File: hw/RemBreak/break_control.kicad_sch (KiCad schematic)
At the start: 13 parts, among them J1 Conn_01x03, J8 Conn_01x07, J9 Conn_01x07, Q1 BC337, Q2 BC847

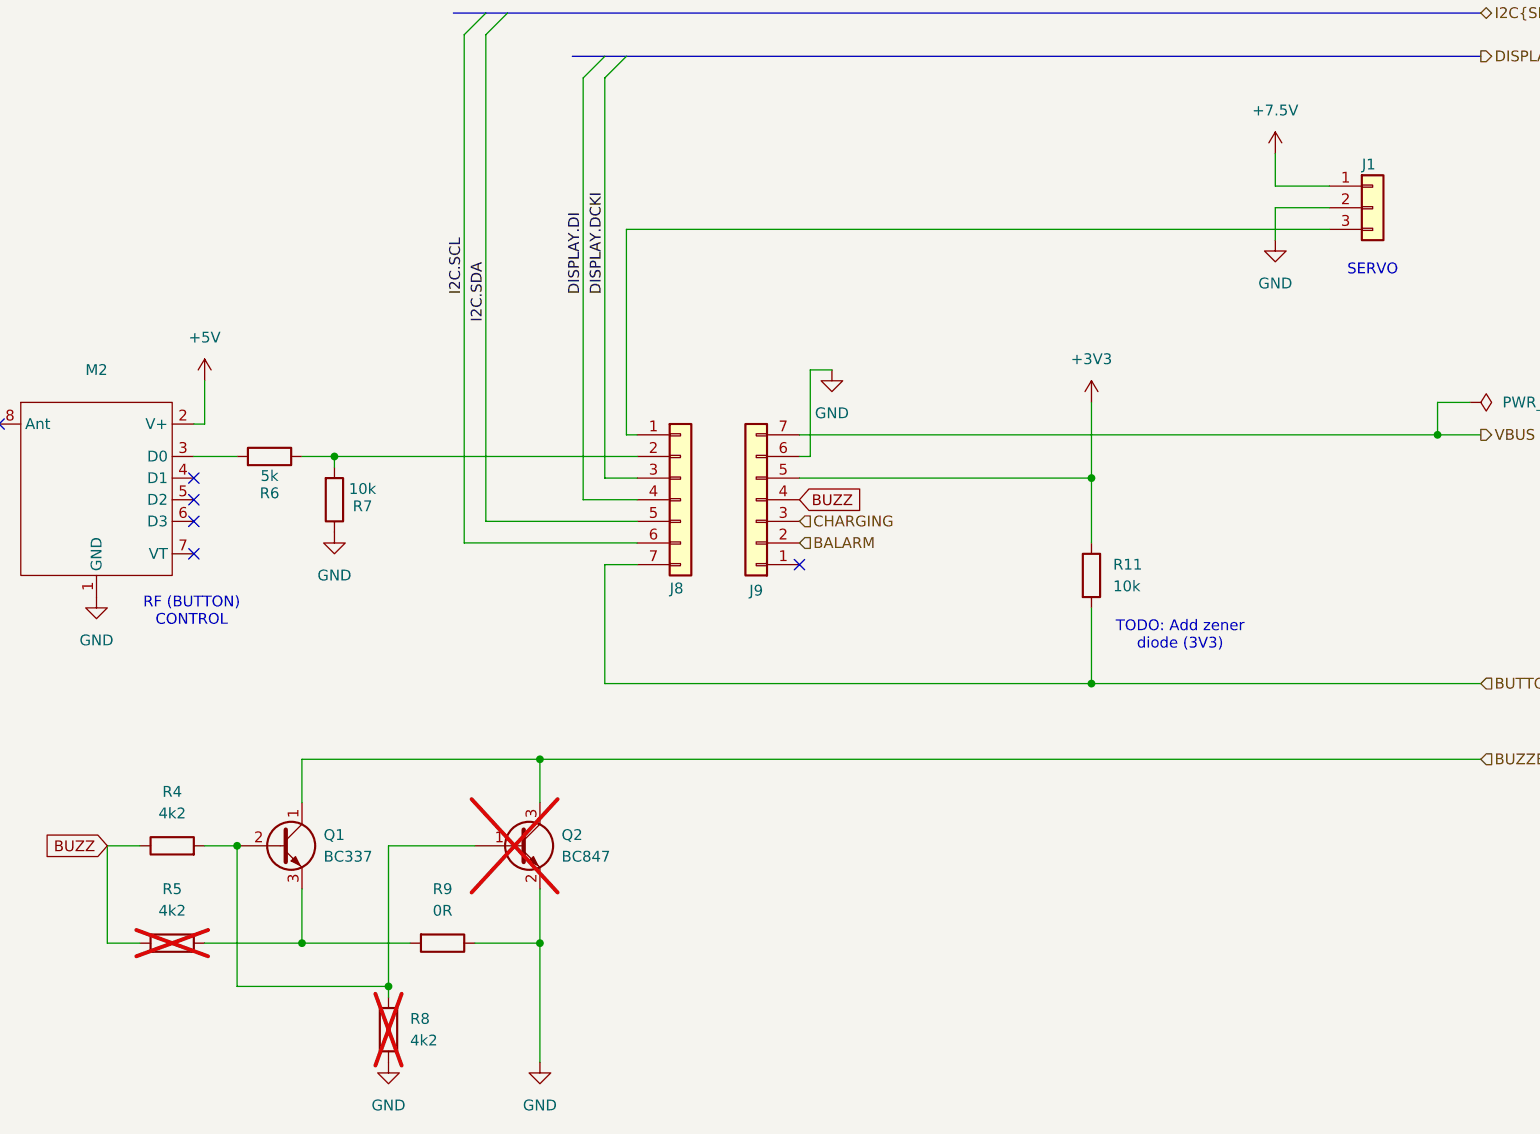
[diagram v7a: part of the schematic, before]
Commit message: regenerated anotations and used battery connector with grounding
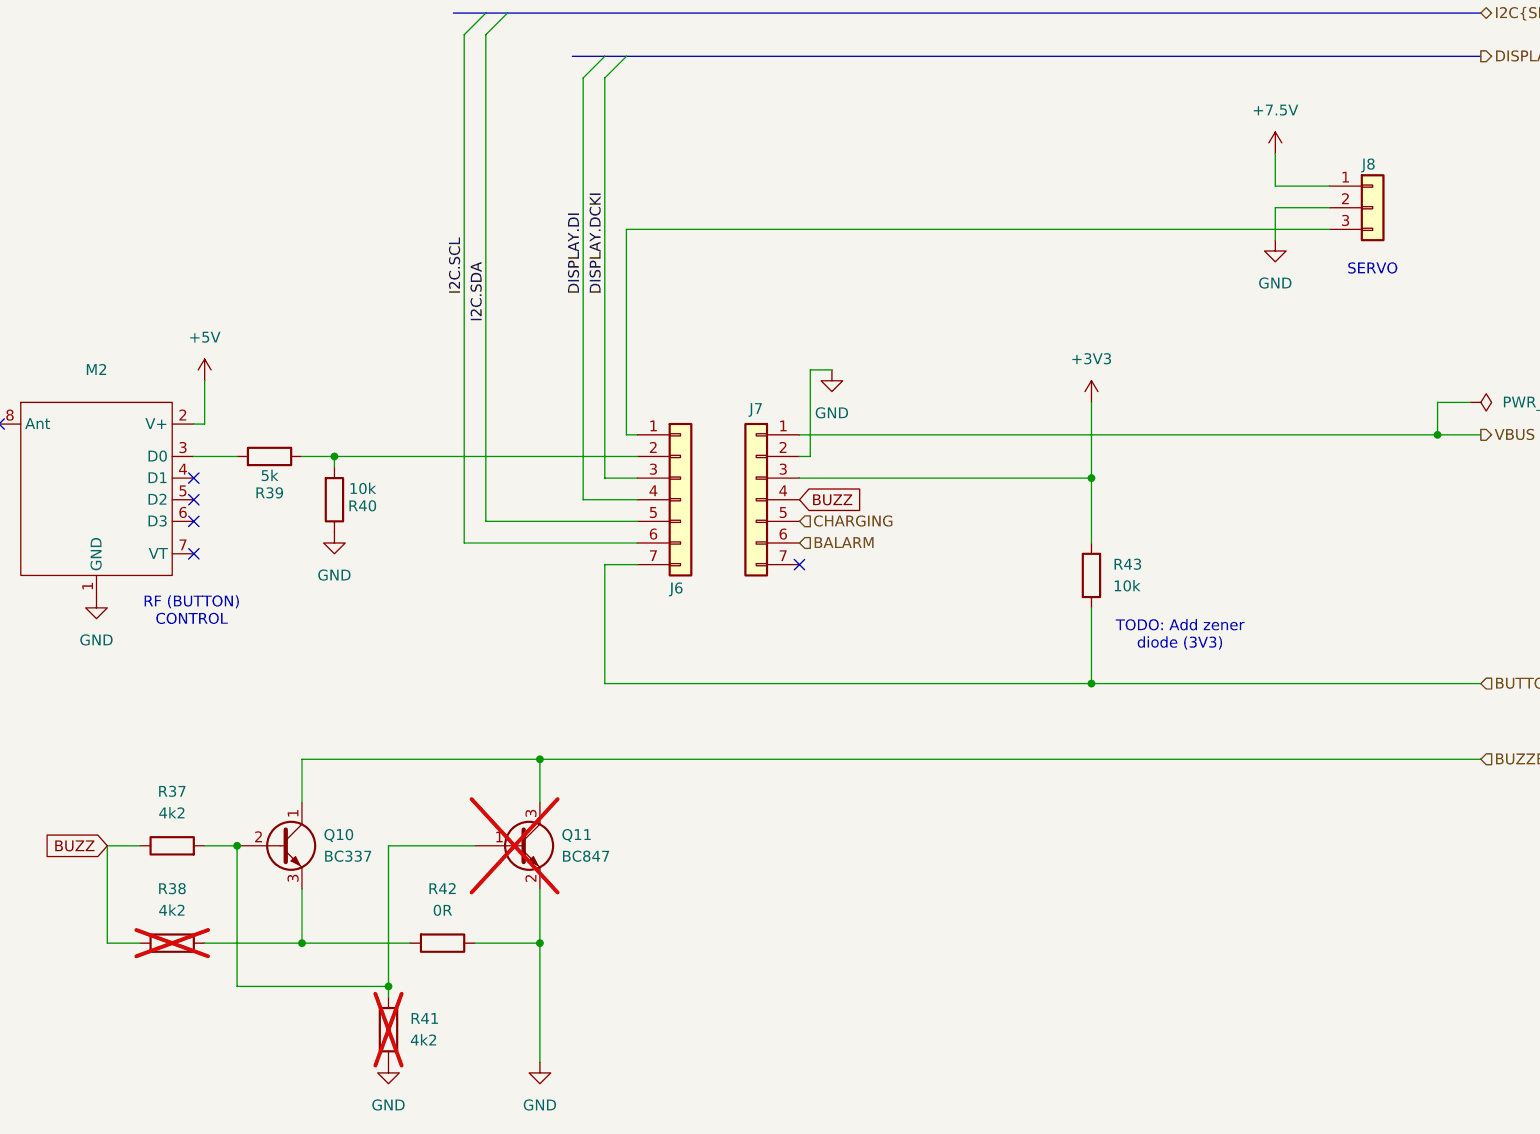
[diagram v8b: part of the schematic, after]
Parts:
- renumbered J8 to J6, J9 to J7, J1 to J8, Q1 to Q10, Q2 to Q11, R4 to R37, R5 to R38, R6 to R39, R7 to R40, R8 to R41, R9 to R42, R11 to R43
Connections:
- net +3V3: now also J7.3 (Pin_3); no longer J7.5 (Pin_5)
- net BALARM: now also J7.6 (Pin_6); no longer J7.2 (Pin_2)
- net CHARGING: now also J7.5 (Pin_5); no longer J7.3 (Pin_3)
- net GND: now also J7.2 (Pin_2); no longer J7.6 (Pin_6)
- net VBUS: now also J7.1 (Pin_1); no longer J7.7 (Pin_7)
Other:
- moved on the sheet: J7
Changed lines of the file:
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@@
 		(on_board yes)
 		(dnp no)
-		(property "Reference" "J1"
+		(property "Reference" "J8"
 			(at 214.63 54.61 0)
 			(effects
@@
 			(project "RemBreak"
 				(path "/e6d4ae5b-c9d7-4cbe-b288-c929fdf55a75/4813b76c-f465-42f9-8515-5ce5d55b4403"
-					(reference "J1")
+					(reference "J8")
 					(unit 1)
 				)
@@
 		(dnp no)
 		(fields_autoplaced yes)
-		(property "Reference" "Q1"
+		(property "Reference" "Q10"
 			(at 92.71 133.3499 0)
 			(effects
@@
 			(project "RemBreak"
 				(path "/e6d4ae5b-c9d7-4cbe-b288-c929fdf55a75/4813b76c-f465-42f9-8515-5ce5d55b4403"
-					(reference "Q1")
+					(reference "Q10")
 					(unit 1)
 				)
@@
 		(dnp no)
 		(fields_autoplaced yes)
-		(property "Reference" "#PWR06"
+		(property "Reference" "#PWR040"
 			(at 118.11 166.37 0)
 			(effects
@@
 			(project "RemBreak"
 				(path "/e6d4ae5b-c9d7-4cbe-b288-c929fdf55a75/4813b76c-f465-42f9-8515-5ce5d55b4403"
-					(reference "#PWR06")
+					(reference "#PWR040")
 					(unit 1)
 				)
@@
 		(dnp no)
 		(fields_autoplaced yes)
-		(property "Reference" "R4"
+		(property "Reference" "R37"
 			(at 74.93 128.27 90)
 			(effects
@@
 			(project "RemBreak"
 				(path "/e6d4ae5b-c9d7-4cbe-b288-c929fdf55a75/4813b76c-f465-42f9-8515-5ce5d55b4403"
-					(reference "R4")
+					(reference "R37")
 					(unit 1)
 				)
@@
 		(dnp no)
 		(fields_autoplaced yes)
-		(property "Reference" "R11"
+		(property "Reference" "R43"
 			(at 185.42 101.5999 0)
 			(effects
@@
 			(project "RemBreak"
 				(path "/e6d4ae5b-c9d7-4cbe-b288-c929fdf55a75/4813b76c-f465-42f9-8515-5ce5d55b4403"
-					(reference "R11")
+					(reference "R43")
 					(unit 1)
 				)
@@
 		(dnp no)
 		(fields_autoplaced yes)
-		(property "Reference" "#PWR017"
+		(property "Reference" "#PWR042"
 			(at 182.88 86.36 0)
 			(effects
@@
 			(project ""
 				(path "/e6d4ae5b-c9d7-4cbe-b288-c929fdf55a75/4813b76c-f465-42f9-8515-5ce5d55b4403"
-					(reference "#PWR017")
+					(reference "#PWR042")
 					(unit 1)
 				)
@@
 		(dnp yes)
 		(fields_autoplaced yes)
-		(property "Reference" "Q2"
+		(property "Reference" "Q11"
 			(at 120.65 133.3499 0)
 			(effects
@@
 			(project "RemBreak"
 				(path "/e6d4ae5b-c9d7-4cbe-b288-c929fdf55a75/4813b76c-f465-42f9-8515-5ce5d55b4403"
-					(reference "Q2")
+					(reference "Q11")
 					(unit 1)
 				)
@@
 		(dnp no)
 		(fields_autoplaced yes)
-		(property "Reference" "#PWR022"
+		(property "Reference" "#PWR036"
 			(at 66.04 111.76 0)
 			(effects
@@
 			(project ""
 				(path "/e6d4ae5b-c9d7-4cbe-b288-c929fdf55a75/4813b76c-f465-42f9-8515-5ce5d55b4403"
-					(reference "#PWR022")
+					(reference "#PWR036")
 					(unit 1)
 				)
@@
 	(symbol
 		(lib_id "Connector_Generic:Conn_01x07")
-		(at 143.51 93.98 180)
-		(unit 1)
-		(exclude_from_sim no)
-		(in_bom yes)
-		(on_board yes)
-		(dnp no)
-		(property "Reference" "J9"
-			(at 143.51 104.648 0)
+		(at 143.51 93.98 0)
+		(mirror y)
+		(unit 1)
+		(exclude_from_sim no)
+		(in_bom yes)
+		(on_board yes)
+		(dnp no)
+		(property "Reference" "J7"
+			(at 143.51 83.312 0)
 			(effects
 				(font
@@
 		)
 		(property "Value" "Conn_01x07"
-			(at 143.51 82.55 0)
+			(at 143.51 105.41 0)
 			(effects
 				(font
@@
 			(project "RemBreak"
 				(path "/e6d4ae5b-c9d7-4cbe-b288-c929fdf55a75/4813b76c-f465-42f9-8515-5ce5d55b4403"
-					(reference "J9")
+					(reference "J7")
 					(unit 1)
 				)
@@
 		(dnp no)
 		(fields_autoplaced yes)
-		(property "Reference" "R9"
+		(property "Reference" "R42"
 			(at 106.68 139.7 90)
 			(effects
@@
 			(project "RemBreak"
 				(path "/e6d4ae5b-c9d7-4cbe-b288-c929fdf55a75/4813b76c-f465-42f9-8515-5ce5d55b4403"
-					(reference "R9")
+					(reference "R42")
 					(unit 1)
 				)
@@
 		(dnp no)
 		(fields_autoplaced yes)
-		(property "Reference" "#PWR07"
+		(property "Reference" "#PWR044"
 			(at 204.47 69.85 0)
 			(effects
@@
 			(project "RemBreak"
 				(path "/e6d4ae5b-c9d7-4cbe-b288-c929fdf55a75/4813b76c-f465-42f9-8515-5ce5d55b4403"
-					(reference "#PWR07")
+					(reference "#PWR044")
 					(unit 1)
 				)
@@
 		(dnp no)
 		(fields_autoplaced yes)
-		(property "Reference" "#PWR02"
+		(property "Reference" "#PWR038"
 			(at 93.98 104.14 0)
 			(effects
@@
 			(project "RemBreak"
 				(path "/e6d4ae5b-c9d7-4cbe-b288-c929fdf55a75/4813b76c-f465-42f9-8515-5ce5d55b4403"
-					(reference "#PWR02")
+					(reference "#PWR038")
 					(unit 1)
 				)
@@
 		(dnp yes)
 		(fields_autoplaced yes)
-		(property "Reference" "R5"
+		(property "Reference" "R38"
 			(at 74.93 139.7 90)
 			(effects
@@
 			(project "RemBreak"
 				(path "/e6d4ae5b-c9d7-4cbe-b288-c929fdf55a75/4813b76c-f465-42f9-8515-5ce5d55b4403"
-					(reference "R5")
+					(reference "R38")
 					(unit 1)
 				)
@@
 		(on_board yes)
 		(dnp no)
-		(property "Reference" "J8"
+		(property "Reference" "J6"
 			(at 133.35 104.394 0)
 			(effects
@@
 			(project "RemBreak"
 				(path "/e6d4ae5b-c9d7-4cbe-b288-c929fdf55a75/4813b76c-f465-42f9-8515-5ce5d55b4403"
-					(reference "J8")
+					(reference "J6")
 					(unit 1)
 				)
@@
 		(dnp no)
 		(fields_autoplaced yes)
-		(property "Reference" "#PWR035"
+		(property "Reference" "#PWR037"
 			(at 78.74 83.82 0)
 			(effects
@@
 			(project ""
 				(path "/e6d4ae5b-c9d7-4cbe-b288-c929fdf55a75/4813b76c-f465-42f9-8515-5ce5d55b4403"
-					(reference "#PWR035")
+					(reference "#PWR037")
 					(unit 1)
 				)
@@
 		(dnp no)
 		(fields_autoplaced yes)
-		(property "Reference" "#PWR09"
+		(property "Reference" "#PWR041"
 			(at 152.4 85.09 0)
 			(effects
@@
 			(project "RemBreak"
 				(path "/e6d4ae5b-c9d7-4cbe-b288-c929fdf55a75/4813b76c-f465-42f9-8515-5ce5d55b4403"
-					(reference "#PWR09")
+					(reference "#PWR041")
 					(unit 1)
 				)
@@
 		(dnp no)
 		(fields_autoplaced yes)
-		(property "Reference" "#FLG08"
+		(property "Reference" "#FLG07"
 			(at 229.235 82.55 0)
 			(effects
@@
 			(project "RemBreak"
 				(path "/e6d4ae5b-c9d7-4cbe-b288-c929fdf55a75/4813b76c-f465-42f9-8515-5ce5d55b4403"
-					(reference "#FLG08")
+					(reference "#FLG07")
 					(unit 1)
 				)
@@
 		(dnp no)
 		(fields_autoplaced yes)
-		(property "Reference" "#PWR03"
+		(property "Reference" "#PWR039"
 			(at 100.33 166.37 0)
 			(effects
@@
 			(project "RemBreak"
 				(path "/e6d4ae5b-c9d7-4cbe-b288-c929fdf55a75/4813b76c-f465-42f9-8515-5ce5d55b4403"
-					(reference "#PWR03")
+					(reference "#PWR039")
 					(unit 1)
 				)
@@
 		(dnp yes)
 		(fields_autoplaced yes)
-		(property "Reference" "R8"
+		(property "Reference" "R41"
 			(at 102.87 154.9399 0)
 			(effects
@@
 			(project "RemBreak"
 				(path "/e6d4ae5b-c9d7-4cbe-b288-c929fdf55a75/4813b76c-f465-42f9-8515-5ce5d55b4403"
-					(reference "R8")
+					(reference "R41")
 					(unit 1)
 				)
@@
 		(on_board yes)
 		(dnp no)
-		(property "Reference" "R6"
+		(property "Reference" "R39"
 			(at 86.36 93.218 90)
 			(effects
@@
 			(project "RemBreak"
 				(path "/e6d4ae5b-c9d7-4cbe-b288-c929fdf55a75/4813b76c-f465-42f9-8515-5ce5d55b4403"
-					(reference "R6")
+					(reference "R39")
 					(unit 1)
 				)
@@
 		(dnp no)
 		(fields_autoplaced yes)
-		(property "Reference" "#PWR012"
+		(property "Reference" "#PWR043"
 			(at 204.47 57.15 0)
 			(effects
@@
 			(project ""
 				(path "/e6d4ae5b-c9d7-4cbe-b288-c929fdf55a75/4813b76c-f465-42f9-8515-5ce5d55b4403"
-					(reference "#PWR012")
+					(reference "#PWR043")
 					(unit 1)
 				)
@@
 		(on_board yes)
 		(dnp no)
-		(property "Reference" "R7"
+		(property "Reference" "R40"
 			(at 97.282 94.742 0)
 			(effects
@@
 			(project "RemBreak"
 				(path "/e6d4ae5b-c9d7-4cbe-b288-c929fdf55a75/4813b76c-f465-42f9-8515-5ce5d55b4403"
-					(reference "R7")
-					(unit 1)
-				)
+					(reference "R40")
+					(unit 1)
+				)
